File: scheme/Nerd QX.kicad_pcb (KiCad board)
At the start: 6 copper layers, 89 x 184 mm, 263 parts, among them J1 Connector 02x01, J2 Conn_01x04, M1 Fan_4pin, M2 Fan_4pin, M3 Fan_4pin, U10 CSD95472Q5MC, U19 BM1370_mode1, U2 TMUX1109RSVR, U20 BM1370_mode1, U25 BM1370_mode1, U26 BM1370_mode1, U3 TPS53647, U30 T-Display-S3, U32 EMC2302-1, U33 TXU0102-DCU, U35 TXU0304PW, U36 MCP1824T-1202E, U37 TMP1075, U38 TMP1075, U4 CSD95472Q5MC, U5 TMP451, U6 AP3211, U7 MCP1824T-0802E, U8 25MHz, U9 CSD95472Q5MC

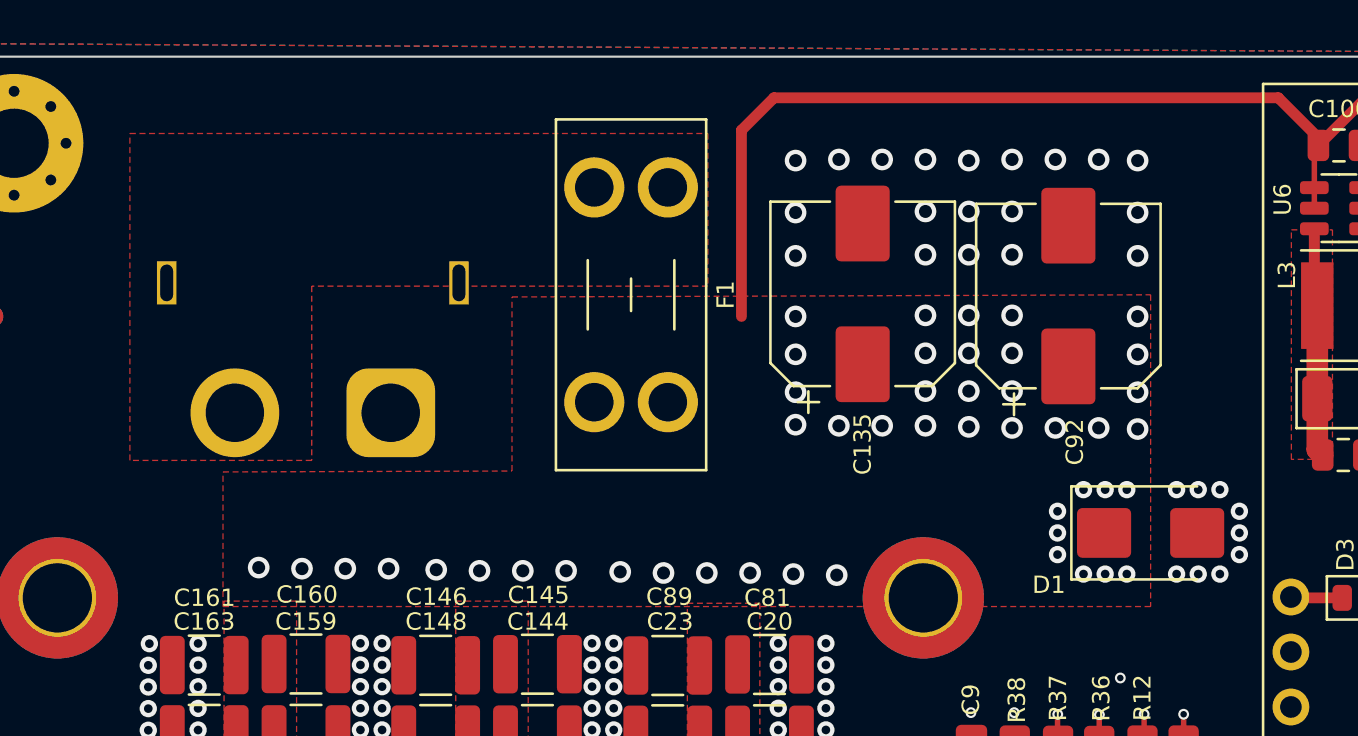
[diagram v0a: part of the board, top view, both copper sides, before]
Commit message: Revert "Moved J1 XT60 connector from top to bottom side of the board. Exported new gerber files, drill files and P&P files. Exported new PCB STEP file."
This reverts commit 3dc59e0cc8feb32dc6b1378662933946a2f0176a.
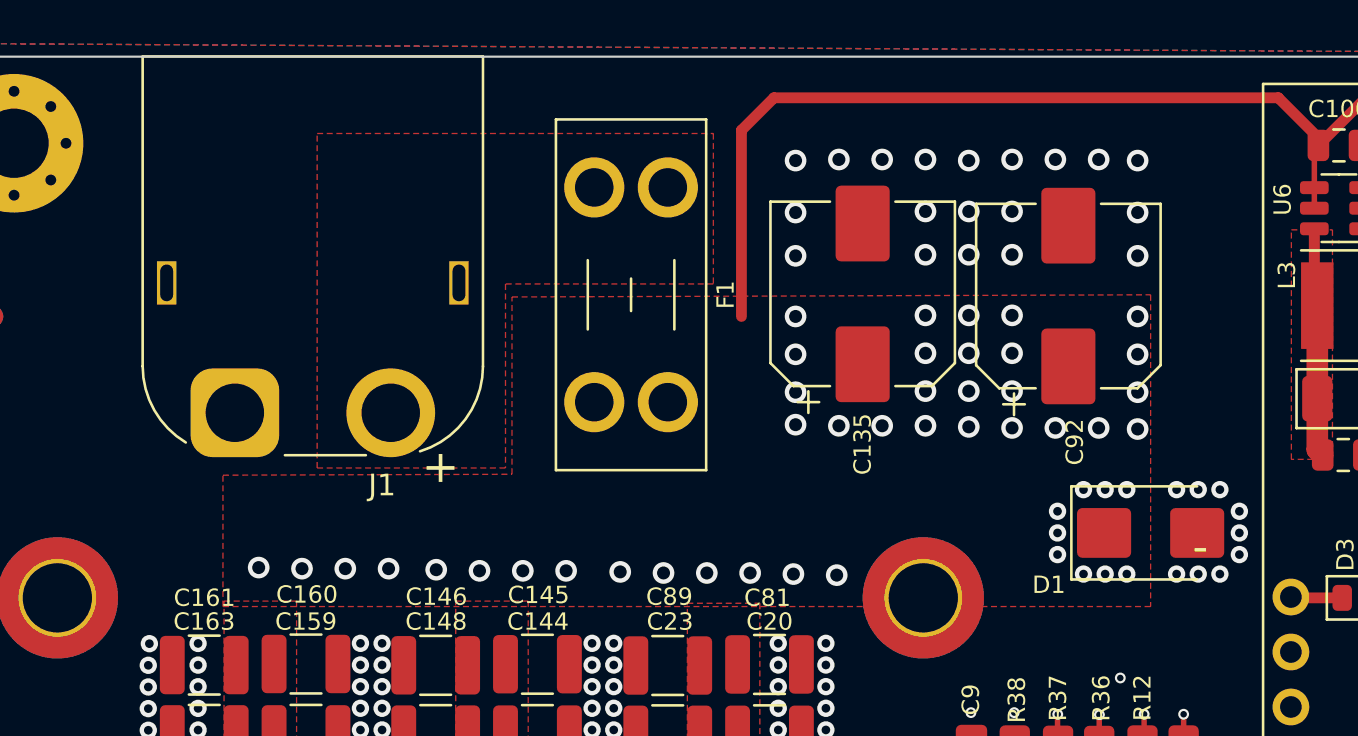
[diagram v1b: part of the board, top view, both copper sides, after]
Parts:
- J1: moved to F.Cu
- moved J1 7.20 mm to (63.2, 29.4), turned to 0 degrees
